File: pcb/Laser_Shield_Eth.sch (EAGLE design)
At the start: 61 parts, among them IC1 CAT811TTBI-CT3, IC11 74LVC1G14DBV, IC2 MC33269ST-3, IC3 MC33269D-3, IC4 W5100, J4 JUMPER_SOLDER_1X2, Q1 25MHz, U1 SN74LVC2G241DCUT, X1 22-23-2031, X2 22-23-2031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

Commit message: pcb done?
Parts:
- removed FULLD: (no value), led:LEDCHIPLED_0805
- removed X1, X2, X3: 22-23-2031, con-molex:22-23-2031
- added CAM, LASER, SERVO: 22-23-2031, con-molex:22-23-2031
- added J5, J6: JUMPER_SOLDER_1X2, parts:JUMPER_SOLDER_1X2
- added Q2: MOSFET-NCHANNELSMD, SparkFun-DiscreteSemi:MOSFET-NCHANNELSMD
- added R13: 100k, SmartPrj:R-EU_R0603
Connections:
- new net N$13: J6.2, Q2.G, R13.2
- new net N$14: J5.2, LASER-1.S, Q2.D
- new net N$15: J1.6, RN1A.1
- net +12V: now also CAM-3.S, SERVO-2.S; no longer X1-2.S, X3-3.S
- net +5V: now also LASER-3.S; no longer X2-3.S
- net CAM_TRIG: now also CAM-2.S; no longer X3-2.S
- net GND: now also CAM-1.S, J5.1, Q2.S, R13.1, SERVO-1.S; no longer X1-1.S, X2-1.S, X3-1.S
- net LASER_CTRL: now also J6.1, LASER-2.S; no longer X2-2.S
- net SCK: no longer RN1A.1
- net SERVO_DATA: now also SERVO-3.S; no longer X1-3.S
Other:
- moved on the sheet: C1, C10, C16, C2, C3, C4, C5, C8, C9, CMD, IC1, IC11P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

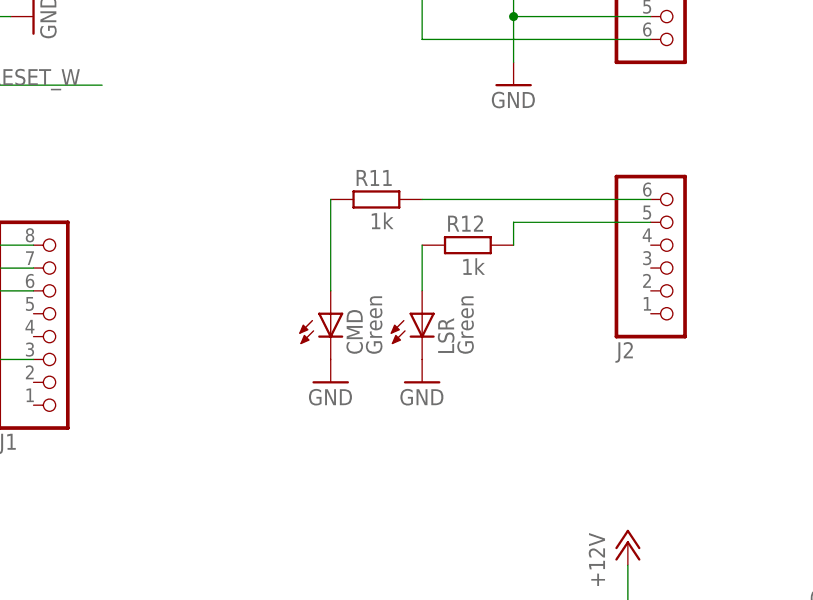
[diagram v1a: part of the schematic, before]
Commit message: pcb: more LEDS
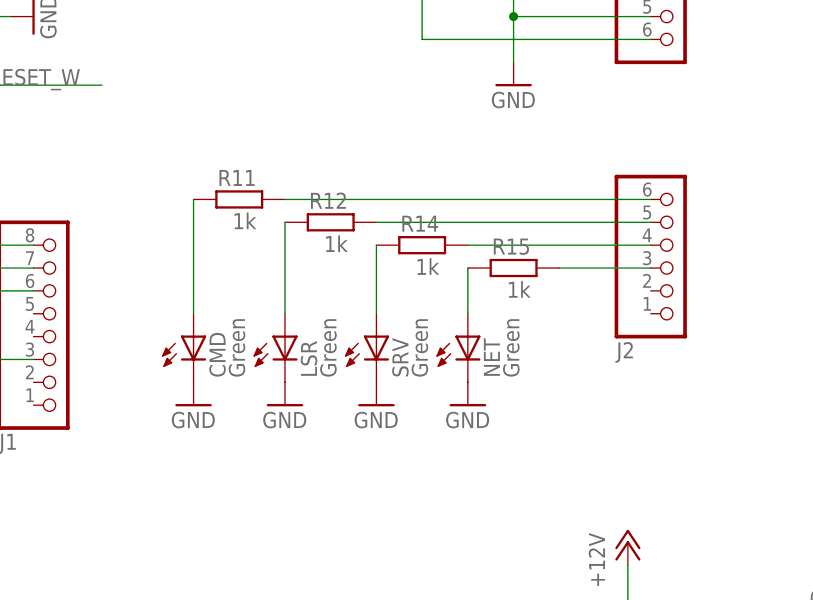
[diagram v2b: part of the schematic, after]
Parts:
- added NET, SRV: Green, led:LEDCHIPLED_0805
- added R14, R15: 1k, SmartPrj:R-EU_R0603
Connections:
- new net N$11: R14.1, SRV.A
- new net N$12: NET.A, R15.1
- new net N$19: J2.4, R14.2
- new net N$20: J2.3, R15.2
- net GND: now also NET.C, SRV.C
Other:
- moved on the sheet: CMD, LSR, R11, R12

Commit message: final pcb eth socket fixes
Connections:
- net +3V3A: now also U$1.RCT, U$1.TCT; no longer U$1.CT
- net V1+: now also U$1.PA+; no longer U$1.SPARE2
- net V1-: now also U$1.PA-; no longer U$1.SPARE1
- net V2+: now also U$1.PB+; no longer U$1.RXCT
- net V2-: now also U$1.PB-; no longer U$1.TXCT
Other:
- note added: "Ethernet Jack = TE 1-6605310-1 (Farnell 1630004)"
- note added: "PoE Module = PEM1312 (Farnell 1902525)"
- moved on the sheet: RN2A, RN2B
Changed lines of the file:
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@@
 <text x="325.12" y="66.04" size="3.81" layer="94">PoE Module</text>
 <text x="335.28" y="60.96" size="3.81" layer="94">tbd</text>
+<text x="193.04" y="-30.48" size="1.778" layer="91">PoE Module = PEM1312 (Farnell 1902525)</text>
+<text x="193.04" y="-33.02" size="1.778" layer="91">Ethernet Jack = TE 1-6605310-1 (Farnell 1630004)</text>
 </plain>
 <instances>
@@
 <attribute name="VALUE" x="86.741" y="157.48" size="1.778" layer="96"/>
 </instance>
-<instance part="GND17" gate="1" x="93.98" y="152.4" smashed="yes">
-<attribute name="VALUE" x="91.44" y="149.86" size="1.778" layer="96"/>
+<instance part="GND17" gate="1" x="93.98" y="154.94" smashed="yes">
+<attribute name="VALUE" x="91.44" y="152.4" size="1.778" layer="96"/>
 </instance>
 <instance part="C5" gate="G$1" x="307.34" y="5.08" smashed="yes">
@@
 <instance part="C6" gate="G$1" x="187.96" y="66.04" rot="R90"/>
 <instance part="C7" gate="G$1" x="187.96" y="40.64" rot="R90"/>
-<instance part="RN2" gate="A" x="99.06" y="165.1"/>
-<instance part="RN2" gate="B" x="86.36" y="165.1" rot="R180"/>
+<instance part="RN2" gate="A" x="99.06" y="167.64"/>
+<instance part="RN2" gate="B" x="86.36" y="167.64" rot="R180"/>
 <instance part="RN2" gate="C" x="127" y="175.26"/>
 <instance part="RN2" gate="D" x="114.3" y="175.26" rot="R180"/>
@@
 </segment>
 <segment>
-<wire x1="93.98" y1="157.48" x2="93.98" y2="154.94" width="0.1524" layer="91"/>
 <pinref part="C4" gate="G$1" pin="1"/>
 <pinref part="GND17" gate="1" pin="GND"/>
@@
 <net name="N$29" class="0">
 <segment>
-<wire x1="93.98" y1="165.1" x2="91.44" y2="165.1" width="0.1524" layer="91"/>
-<junction x="93.98" y="165.1"/>
+<wire x1="93.98" y1="167.64" x2="91.44" y2="167.64" width="0.1524" layer="91"/>
+<junction x="93.98" y="167.64"/>
 <pinref part="C4" gate="G$1" pin="2"/>
 <pinref part="RN2" gate="B" pin="1"/>
 <pinref part="RN2" gate="A" pin="1"/>
+<wire x1="93.98" y1="167.64" x2="93.98" y2="165.1" width="0.1524" layer="91"/>
 </segment>
 </net>
@@
 <wire x1="43.18" y1="177.8" x2="134.62" y2="177.8" width="0.1524" layer="91"/>
 <wire x1="43.18" y1="177.8" x2="43.18" y2="160.02" width="0.1524" layer="91"/>
-<wire x1="43.18" y1="160.02" x2="20.32" y2="160.02" width="0.1524" layer="91"/>
 <junction x="134.62" y="175.26"/>
 <label x="137.795" y="175.26" size="1.778" layer="95"/>
 <pinref part="RN2" gate="C" pin="2"/>
 <pinref part="U$1" gate="G$1" pin="TD+"/>
+<wire x1="43.18" y1="160.02" x2="20.32" y2="160.02" width="0.1524" layer="91"/>
 </segment>
 </net>
 <net name="RXIP" class="0">
 <segment>
-<wire x1="106.68" y1="170.18" x2="106.68" y2="165.1" width="0.1524" layer="91"/>
-<wire x1="106.68" y1="165.1" x2="106.68" y2="152.4" width="0.1524" layer="91"/>
+<wire x1="106.68" y1="170.18" x2="106.68" y2="167.64" width="0.1524" layer="91"/>
+<wire x1="106.68" y1="167.64" x2="106.68" y2="152.4" width="0.1524" layer="91"/>
 <wire x1="106.68" y1="152.4" x2="144.78" y2="152.4" width="0.1524" layer="91"/>
-<wire x1="104.14" y1="165.1" x2="106.68" y2="165.1" width="0.1524" layer="91"/>
+<wire x1="104.14" y1="167.64" x2="106.68" y2="167.64" width="0.1524" layer="91"/>
 <wire x1="106.68" y1="170.18" x2="20.32" y2="170.18" width="0.1524" layer="91"/>
-<junction x="106.68" y="165.1"/>
+<junction x="106.68" y="167.64"/>
 <label x="137.795" y="152.4" size="1.778" layer="95"/>
 <pinref part="RN2" gate="A" pin="2"/>
@@
 <segment>
 <wire x1="144.78" y1="149.86" x2="81.28" y2="149.86" width="0.1524" layer="91"/>
-<wire x1="81.28" y1="149.86" x2="81.28" y2="165.1" width="0.1524" layer="91"/>
-<wire x1="81.28" y1="165.1" x2="55.88" y2="165.1" width="0.1524" layer="91"/>
-<wire x1="55.88" y1="165.1" x2="55.88" y2="167.64" width="0.1524" layer="91"/>
-<wire x1="55.88" y1="167.64" x2="20.32" y2="167.64" width="0.1524" layer="91"/>
-<junction x="81.28" y="165.1"/>
+<wire x1="81.28" y1="149.86" x2="81.28" y2="167.64" width="0.1524" layer="91"/>
+<wire x1="81.28" y1="167.64" x2="20.32" y2="167.64" width="0.1524" layer="91"/>
+<junction x="81.28" y="167.64"/>
 <label x="137.795" y="149.86" size="1.778" layer="95"/>
 <pinref part="RN2" gate="B" pin="2"/>
@@
 <wire x1="48.26" y1="172.72" x2="109.22" y2="172.72" width="0.1524" layer="91"/>
 <wire x1="48.26" y1="172.72" x2="48.26" y2="162.56" width="0.1524" layer="91"/>
-<wire x1="48.26" y1="162.56" x2="20.32" y2="162.56" width="0.1524" layer="91"/>
 <junction x="109.22" y="172.72"/>
 <label x="137.795" y="157.48" size="1.778" layer="95"/>
 <pinref part="RN2" gate="D" pin="2"/>
 <pinref part="U$1" gate="G$1" pin="TD-"/>
+<wire x1="48.26" y1="162.56" x2="20.32" y2="162.56" width="0.1524" layer="91"/>
 </segment>
 <segment>
@@
 <wire x1="86.36" y1="175.26" x2="45.72" y2="175.26" width="0.1524" layer="91"/>
 <wire x1="45.72" y1="175.26" x2="45.72" y2="165.1" width="0.1524" layer="91"/>
-<wire x1="45.72" y1="165.1" x2="20.32" y2="165.1" width="0.1524" layer="91"/>
 <junction x="86.36" y="175.26"/>
 <label x="93.98" y="175.26" size="1.778" layer="95"/>
 <pinref part="C1" gate="G$1" pin="1"/>
-<pinref part="U$1" gate="G$1" pin="CT"/>
+<label x="22.86" y="165.1" size="1.778" layer="95"/>
+<pinref part="U$1" gate="G$1" pin="RCT"/>
+<wire x1="45.72" y1="165.1" x2="22.86" y2="165.1" width="0.1524" layer="91"/>
+<pinref part="U$1" gate="G$1" pin="TCT"/>
+<wire x1="22.86" y1="165.1" x2="20.32" y2="165.1" width="0.1524" layer="91"/>
+<wire x1="20.32" y1="157.48" x2="22.86" y2="157.48" width="0.1524" layer="91"/>
+<wire x1="22.86" y1="157.48" x2="22.86" y2="165.1" width="0.1524" layer="91"/>
+<junction x="22.86" y="165.1"/>
 </segment>
 <segment>
@@
 </segment>
 <segment>
-<wire x1="27.94" y1="147.32" x2="20.32" y2="147.32" width="0.1524" layer="91"/>
-<label x="22.86" y="147.32" size="1.778" layer="95"/>
-<pinref part="U$1" gate="G$1" pin="SPARE2"/>
+<pinref part="U$1" gate="G$1" pin="PA+"/>
+<wire x1="20.32" y1="149.86" x2="27.94" y2="149.86" width="0.1524" layer="91"/>
+<label x="22.86" y="149.86" size="1.778" layer="95"/>
 </segment>
 </net>
@@
 </segment>
 <segment>
-<wire x1="27.94" y1="149.86" x2="20.32" y2="149.86" width="0.1524" layer="91"/>
-<label x="22.86" y="149.86" size="1.778" layer="95"/>
-<pinref part="U$1" gate="G$1" pin="SPARE1"/>
+<pinref part="U$1" gate="G$1" pin="PA-"/>
+<wire x1="20.32" y1="147.32" x2="27.94" y2="147.32" width="0.1524" layer="91"/>
+<label x="22.86" y="147.32" size="1.778" layer="95"/>
 </segment>
 </net>
@@
 <wire x1="27.94" y1="154.94" x2="20.32" y2="154.94" width="0.1524" layer="91"/>
 <label x="22.86" y="154.94" size="1.778" layer="95"/>
-<pinref part="U$1" gate="G$1" pin="RXCT"/>
+<pinref part="U$1" gate="G$1" pin="PB+"/>
 </segment>
 </net>
@@
 <wire x1="27.94" y1="152.4" x2="20.32" y2="152.4" width="0.1524" layer="91"/>
 <label x="22.86" y="152.4" size="1.778" layer="95"/>
-<pinref part="U$1" gate="G$1" pin="TXCT"/>
-</segment>
-</net>
+<pinref part="U$1" gate="G$1" pin="PB-"/>
+</segment>
+</net>

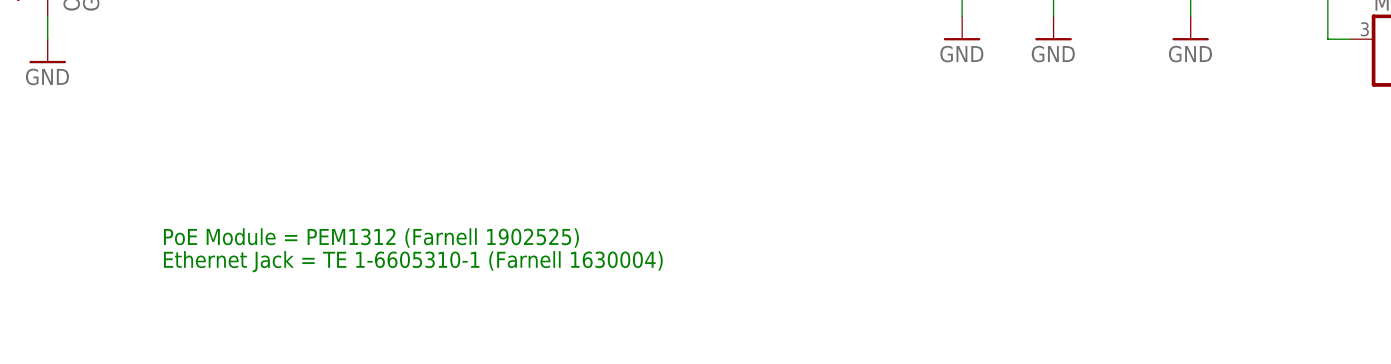
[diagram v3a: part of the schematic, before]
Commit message: pcb: more part numbers
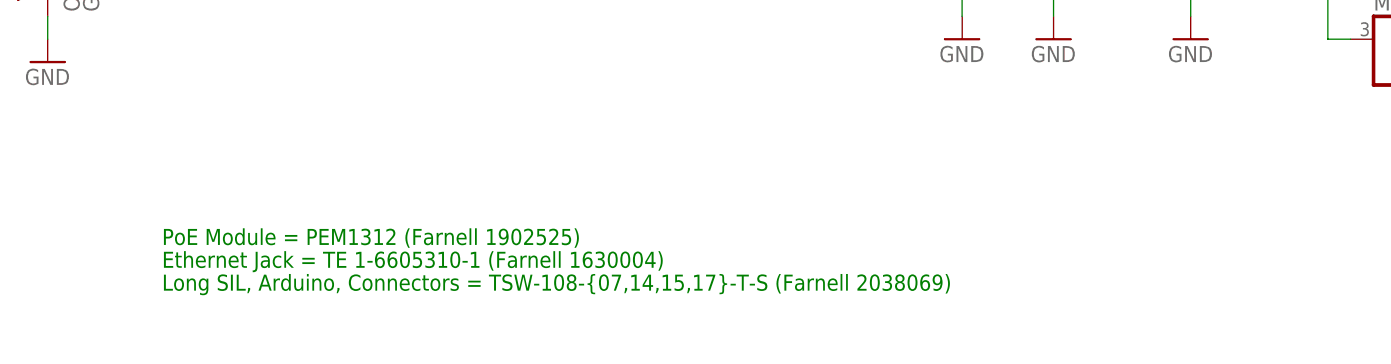
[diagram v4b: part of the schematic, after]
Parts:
- IC1: MPN (none) -> STM812LW16F; OC_FARNELL (none) -> 8690545
- IC11: MPN (none) -> SN74LVC1G14DBVT; OC_FARNELL (none) -> 1236328
- IC2: OC_FARNELL (none) -> 1652295
- RN1, RN3: MPN (none) -> CAY16-102J4LF; OC_FARNELL (none) -> 1770133
- RN2: MPN (none) -> CAY16-49R9F4LF; OC_FARNELL (none) -> 2113092
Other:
- note added: "Long SIL, Arduino, Connectors = TSW-108-{07,14,15,17}-T-S (Farnell 2038069)"
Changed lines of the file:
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@@
 <part name="R6" library="SmartPrj" deviceset="R-EU_" device="0603-RND" value="N.M."/>
 <part name="GND33" library="supply1" deviceset="GND" device=""/>
-<part name="IC1" library="SmartPrj" deviceset="STM812" device="" value="CAT811TTBI-CT3"/>
+<part name="IC1" library="SmartPrj" deviceset="STM812" device="" value="CAT811TTBI-CT3">
+<attribute name="MPN" value="STM812LW16F"/>
+<attribute name="OC_FARNELL" value="8690545"/>
+</part>
 <part name="GND34" library="supply1" deviceset="GND" device=""/>
 <part name="P+7" library="supply1" deviceset="+5V" device=""/>
@@
 <part name="+3V1" library="supply1" deviceset="+3V3" device=""/>
 <part name="GND42" library="supply1" deviceset="GND" device=""/>
-<part name="RN1" library="resistor-dil" deviceset="4R-N" device="CAY16" value="1k"/>
-<part name="RN3" library="resistor-dil" deviceset="4R-N" device="CAY16" value="1k"/>
+<part name="RN1" library="resistor-dil" deviceset="4R-N" device="CAY16" value="1k">
+<attribute name="MPN" value="CAY16-102J4LF"/>
+<attribute name="OC_FARNELL" value="1770133"/>
+</part>
+<part name="RN3" library="resistor-dil" deviceset="4R-N" device="CAY16" value="1k">
+<attribute name="MPN" value="CAY16-102J4LF"/>
+<attribute name="OC_FARNELL" value="1770133"/>
+</part>
 <part name="Q1" library="special" deviceset="XTAL/S" device="" value="25MHz"/>
 <part name="C6" library="SmartPrj" deviceset="C-EU" device="C0603" value="22p"/>
 <part name="C7" library="SmartPrj" deviceset="C-EU" device="C0603" value="22p"/>
-<part name="RN2" library="resistor-dil" deviceset="4R-N" device="CAY16" value="49R9"/>
+<part name="RN2" library="resistor-dil" deviceset="4R-N" device="CAY16" value="49R9">
+<attribute name="MPN" value="CAY16-49R9F4LF"/>
+<attribute name="OC_FARNELL" value="2113092"/>
+</part>
 <part name="U$1" library="SmartPrj" deviceset="POE-RJ45" device=""/>
 <part name="GND4" library="supply1" deviceset="GND" device=""/>
 <part name="+3V8" library="supply1" deviceset="+3V3" device=""/>
-<part name="IC11" library="74xx-little-de" deviceset="74*1G14" device="DBV" technology="LVC"/>
+<part name="IC11" library="74xx-little-de" deviceset="74*1G14" device="DBV" technology="LVC">
+<attribute name="MPN" value="SN74LVC1G14DBVT"/>
+<attribute name="OC_FARNELL" value="1236328"/>
+</part>
 <part name="R7" library="SmartPrj" deviceset="R-EU_" device="0603-RND" value="N.M."/>
 <part name="GND14" library="supply1" deviceset="GND" device=""/>
@@
 <part name="C16" library="SmartPrj" deviceset="C-EU" device="C0603" value="1u"/>
 <part name="GND38" library="supply1" deviceset="GND" device=""/>
-<part name="IC2" library="linear" deviceset="MC33269ST*" device="" technology="-3.3T3" value="MC33269ST-3"/>
+<part name="IC2" library="linear" deviceset="MC33269ST*" device="" technology="-3.3T3" value="MC33269ST-3">
+<attribute name="OC_FARNELL" value="1652295"/>
+</part>
 <part name="IC3" library="linear" deviceset="MC33269?*" device="D" technology="-3.3" value="MC33269D-3"/>
 <part name="GND10" library="supply1" deviceset="GND" device=""/>
@@
 <text x="193.04" y="-30.48" size="1.778" layer="91">PoE Module = PEM1312 (Farnell 1902525)</text>
 <text x="193.04" y="-33.02" size="1.778" layer="91">Ethernet Jack = TE 1-6605310-1 (Farnell 1630004)</text>
+<text x="193.04" y="-35.56" size="1.778" layer="91">Long SIL, Arduino, Connectors = TSW-108-{07,14,15,17}-T-S (Farnell 2038069)</text>
 </plain>
 <instances>
@@
 </instance>
 <instance part="GND33" gate="1" x="320.04" y="66.04" rot="MR90"/>
-<instance part="IC1" gate="G$1" x="220.98" y="132.08" rot="MR0"/>
+<instance part="IC1" gate="G$1" x="220.98" y="132.08" rot="MR0">
+<attribute name="OC_FARNELL" x="220.98" y="132.08" size="1.778" layer="96" rot="MR0" display="off"/>
+<attribute name="MPN" x="220.98" y="132.08" size="1.778" layer="96" rot="MR0" display="off"/>
+</instance>
 <instance part="GND34" gate="1" x="231.14" y="132.08" rot="R90"/>
 <instance part="P+7" gate="1" x="198.12" y="142.24" smashed="yes">
@@
 <instance part="RN1" gate="A" x="195.58" y="114.3"/>
 <instance part="RN1" gate="B" x="157.48" y="35.56" rot="R180"/>
-<instance part="RN1" gate="C" x="157.48" y="43.18" rot="R180"/>
+<instance part="RN1" gate="C" x="157.48" y="43.18" rot="R180">
+<attribute name="MPN" x="157.48" y="43.18" size="1.778" layer="96" rot="R180" display="off"/>
+<attribute name="OC_FARNELL" x="157.48" y="43.18" size="1.778" layer="96" rot="R180" display="off"/>
+</instance>
 <instance part="RN1" gate="D" x="180.34" y="10.16" rot="R270"/>
 <instance part="RN3" gate="A" x="48.26" y="144.78" smashed="yes" rot="R180">
 <attribute name="NAME" x="43.18" y="141.732" size="1.778" layer="95"/>
 <attribute name="VALUE" x="50.8" y="141.732" size="1.778" layer="96"/>
+<attribute name="MPN" x="48.26" y="144.78" size="1.778" layer="96" rot="R180" display="off"/>
+<attribute name="OC_FARNELL" x="48.26" y="144.78" size="1.778" layer="96" rot="R180" display="off"/>
 </instance>
 <instance part="RN3" gate="B" x="157.48" y="12.7" rot="R180"/>
@@
 <instance part="C7" gate="G$1" x="187.96" y="40.64" rot="R90"/>
 <instance part="RN2" gate="A" x="99.06" y="167.64"/>
-<instance part="RN2" gate="B" x="86.36" y="167.64" rot="R180"/>
+<instance part="RN2" gate="B" x="86.36" y="167.64" rot="R180">
+<attribute name="MPN" x="86.36" y="167.64" size="1.778" layer="96" rot="R180" display="off"/>
+<attribute name="OC_FARNELL" x="86.36" y="167.64" size="1.778" layer="96" rot="R180" display="off"/>
+</instance>
 <instance part="RN2" gate="C" x="127" y="175.26"/>
 <instance part="RN2" gate="D" x="114.3" y="175.26" rot="R180"/>
@@
 <attribute name="VALUE" x="60.96" y="152.4" size="1.778" layer="96" rot="R180"/>
 </instance>
-<instance part="IC11" gate="A" x="27.94" y="-33.02"/>
+<instance part="IC11" gate="A" x="27.94" y="-33.02">
+<attribute name="MPN" x="27.94" y="-33.02" size="1.778" layer="96" display="off"/>
+<attribute name="OC_FARNELL" x="27.94" y="-33.02" size="1.778" layer="96" display="off"/>
+</instance>
 <instance part="IC11" gate="P" x="12.7" y="-17.78"/>
 <instance part="R7" gate="G$1" x="312.42" y="40.64" smashed="yes" rot="R270">
@@
 <instance part="C16" gate="G$1" x="292.1" y="7.62"/>
 <instance part="GND38" gate="1" x="180.34" y="-10.16"/>
-<instance part="IC2" gate="G$1" x="335.28" y="7.62"/>
+<instance part="IC2" gate="G$1" x="335.28" y="7.62">
+<attribute name="OC_FARNELL" x="335.28" y="7.62" size="1.778" layer="96" display="off"/>
+</instance>
 <instance part="IC3" gate="G$1" x="335.28" y="-10.16"/>
 <instance part="GND10" gate="1" x="335.28" y="0"/>

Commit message: note some resistor values and add TODO
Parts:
- R11, R12, R14, R15: value 1k -> 68R
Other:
- note added: "TODO: * change 1k rarray to 68R * add newly ordered part numbers"
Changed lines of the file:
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@@
 <?xml version="1.0" encoding="utf-8"?>
 <!DOCTYPE eagle SYSTEM "eagle.dtd">
-<eagle version="6.2">
+<eagle version="6.4">
 <drawing>
 <settings>
@@
 <part name="SRV" library="led" deviceset="LED" device="CHIPLED_0805" value="Green"/>
 <part name="NET" library="led" deviceset="LED" device="CHIPLED_0805" value="Green"/>
-<part name="R11" library="SmartPrj" deviceset="R-EU_" device="R0603" value="1k"/>
-<part name="R12" library="SmartPrj" deviceset="R-EU_" device="R0603" value="1k"/>
-<part name="R14" library="SmartPrj" deviceset="R-EU_" device="R0603" value="1k"/>
-<part name="R15" library="SmartPrj" deviceset="R-EU_" device="R0603" value="1k"/>
+<part name="R11" library="SmartPrj" deviceset="R-EU_" device="R0603" value="68R"/>
+<part name="R12" library="SmartPrj" deviceset="R-EU_" device="R0603" value="68R"/>
+<part name="R14" library="SmartPrj" deviceset="R-EU_" device="R0603" value="68R"/>
+<part name="R15" library="SmartPrj" deviceset="R-EU_" device="R0603" value="68R"/>
 <part name="GND30" library="supply1" deviceset="GND" device=""/>
 <part name="GND36" library="supply1" deviceset="GND" device=""/>
@@
 <text x="193.04" y="-33.02" size="1.778" layer="91">Ethernet Jack = TE 1-6605310-1 (Farnell 1630004)</text>
 <text x="193.04" y="-35.56" size="1.778" layer="91">Long SIL, Arduino, Connectors = TSW-108-{07,14,15,17}-T-S (Farnell 2038069)</text>
+<text x="127" y="-35.56" size="1.778" layer="91">TODO:
+* change 1k rarray to 68R
+* add newly ordered part numbers</text>
 </plain>
 <instances>
@@
 </schematic>
 </drawing>
+<compatibility>
+<note version="6.3" minversion="6.2.2" severity="warning">
+Since Version 6.2.2 text objects can contain more than one line,
+which will not be processed correctly with this version.
+</note>
+</compatibility>
 </eagle>
